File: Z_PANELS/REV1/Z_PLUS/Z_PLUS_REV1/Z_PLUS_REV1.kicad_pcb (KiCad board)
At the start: 4 copper layers, 98 x 98 mm, 47 parts, among them IC1 LTC4316IDD#PBF, J1 F3311A7H121014E200, Q1 BSS138, Q2 BSS138, Q3 MBT2222ADW1T1, Q4 BSS138, Q5 BSS138, Q6 MBT2222ADW1T1, U1 OPT4001DTST, U2 LTC3130EUDC-1-PBF

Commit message: made changes to Z plus board
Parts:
- removed D4: B220, Diode_SMD:D_SMB
- added D5: RB521S30T1G, AA_AUTO_LOADER:SODFL1608X70N, F.Cu at (171.5, 38.3)
- added D6: RB521S30T1G, AA_AUTO_LOADER:SODFL1608X70N, F.Cu at (179.9, 74.4)
- added D7: RB521S30T1G, AA_AUTO_LOADER:SODFL1608X70N, F.Cu at (176.2, 74.4)
- added IC2: SM141K04TFV, AA_AUTO_LOADER:SODFL490150X120N, F.Cu at (202.0, 103.0)
- added IC3: SM141K04TFV, AA_AUTO_LOADER:SODFL490150X120N, F.Cu at (137.8, 101.5)
- added IC4: SM141K04TFV, AA_AUTO_LOADER:SODFL490150X120N, F.Cu at (187.2, 48.1)
- added IC5: SM141K04TFV, AA_AUTO_LOADER:SODFL490150X120N, F.Cu at (186.7, 65.0)
- C1, C2, C3, C4, C5, C6, C7, C8, IC1, J1, L1, Q1, Q2, Q3, Q4, Q5, Q6, R1, R10, R11, R12, R13, R14, R15, R16, R17, R18, R19, R2, R20, R21, R22, R3, R4, R5, R6, R7, R8, R9, U2: moved to B.Cu
- D1, D3: value MBR0540-TP -> RB521S30T1G; footprint AA_AUTO_LOADER:SOD3716X135N -> AA_AUTO_LOADER:SODFL1608X70N
- D2: value B220 -> RB521S30T1G; footprint Diode_SMD:D_SMB -> AA_AUTO_LOADER:SODFL1608X70N; moved to B.Cu
- moved Q1 116.5 mm to (194.1, 61.0), turned to 180 degrees
- moved Q2 116.5 mm to (194.1, 65.4), turned to 180 degrees
- moved Q4 116.5 mm to (194.1, 69.9), turned to 180 degrees
- moved Q5 116.5 mm to (194.1, 74.3), turned to 180 degrees
- moved L1 115.3 mm to (193.5, 54.2), turned to 180 degrees
- moved R19 113.9 mm to (192.8, 49.5), turned to 180 degrees
- moved D2 113.0 mm to (192.4, 39.1), turned to 180 degrees
- moved R1 108.7 mm to (190.2, 59.8), turned to 180 degrees
- moved R10 108.7 mm to (190.2, 71.7), turned to 180 degrees
- moved R17 108.7 mm to (190.2, 73.7), turned to 180 degrees
- moved R2 108.7 mm to (190.2, 61.8), turned to 180 degrees
- moved R3 108.7 mm to (190.2, 63.7), turned to 180 degrees
- moved R4 108.7 mm to (190.2, 65.7), turned to 180 degrees
- moved R5 108.7 mm to (190.2, 67.7), turned to 180 degrees
- moved R6 108.7 mm to (190.2, 69.7), turned to 180 degrees
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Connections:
- C3 pad 2: Net-(D2-K) -> Net-(U2-PVIN)
- C4 pad 2: Net-(D2-K) -> Net-(U2-PVIN)
- C8 pad 2: Net-(D4-A) -> Net-(U2-VOUT)
- D1 pad 1: /SOLAR_PANEL_ELECTRONICS/7023_vout -> Net-(IC2-NEG)
- D1 pad 2: Net-(S1-Neg) -> Net-(IC3-NEG)
- D2 pad 1: Net-(D2-K) -> VSOLAR
- D2 pad 2: /SOLAR_PANEL_ELECTRONICS/7023_vout -> Net-(U2-VOUT)
- D3 pad 1: Net-(S1-Neg) -> /SOLAR_PANEL_ELECTRONICS/7023_vout
- D3 pad 2: GND -> Net-(IC2-NEG)
- J1 pad 12: VBATT -> unconnected-(J1-Pad12)
- J1 pad 13: VBATT -> unconnected-(J1-Pad13)
- J1 pad 2: VBATT -> unconnected-(J1-Pad2)
- J1 pad 3: VBATT -> unconnected-(J1-Pad3)
- R19 pad 2: Net-(D2-K) -> Net-(U2-PVIN)
- R21 pad 2: Net-(D4-A) -> Net-(U2-VOUT)
- U2 pad 14: Net-(D4-A) -> Net-(U2-VOUT)
- U2 pad 2: Net-(D2-K) -> Net-(U2-PVIN)
- U2 pad 3: Net-(D2-K) -> Net-(U2-PVIN)
- U2 pad 4: Net-(D2-K) -> Net-(U2-PVIN)
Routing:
- net Net-(IC2-NEG): track 0.00 -> 146.3 mm
- net Net-(IC3-NEG): track 0.00 -> 103.9 mm
- net Net-(IC4-NEG): track 0.00 -> 88.7 mm
- net GND: track 0.00 -> 20.9 mm
- net /SOLAR_PANEL_ELECTRONICS/7023_vout: track 0.00 -> 9.60 mm
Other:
- outline, holes or cut-outs redrawn

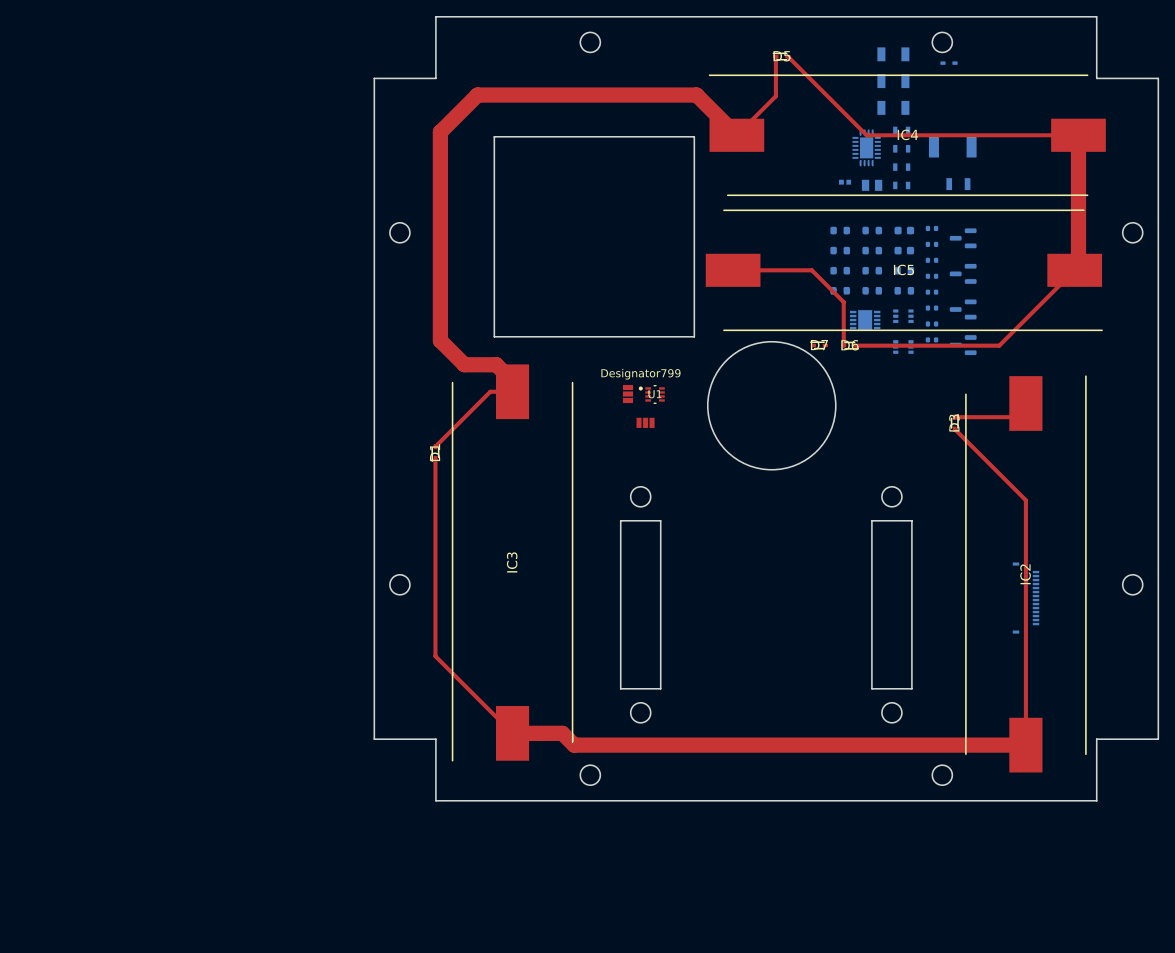
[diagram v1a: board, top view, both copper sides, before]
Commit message: initial routing z plus
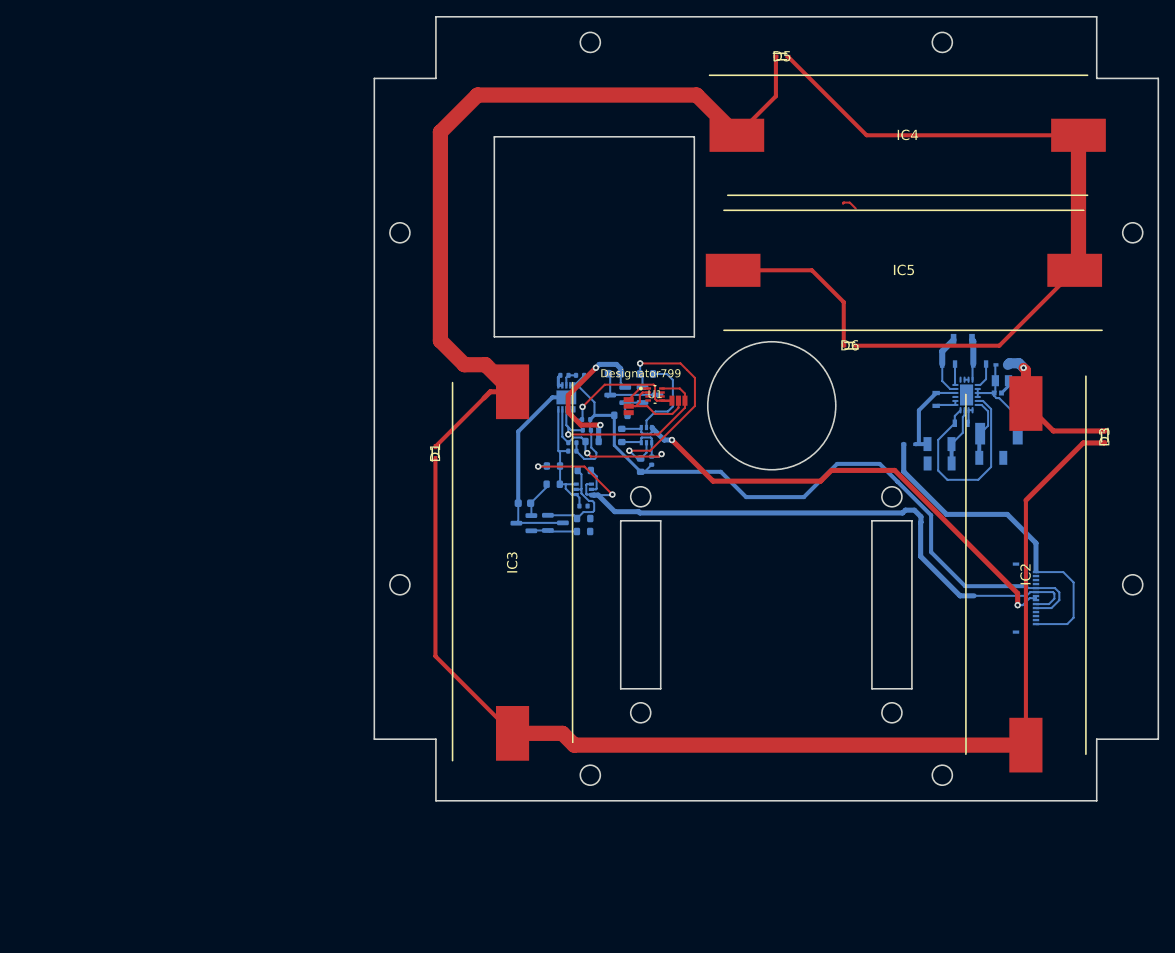
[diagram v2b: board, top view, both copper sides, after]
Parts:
- D7: moved to B.Cu
- moved Q2 63.1 mm to (139.2, 96.6)
- moved Q1 62.2 mm to (143.2, 96.6), turned to 0 degrees
- moved C1 58.4 mm to (139.3, 94.1)
- moved R20 51.9 mm to (197.6, 88.4)
- moved R7 51.7 mm to (146.7, 97.6), turned to 0 degrees
- moved R9 51.0 mm to (146.7, 96.0)
- moved R1 49.5 mm to (144.3, 78.1)
- moved R11 49.4 mm to (142.9, 91.7), turned to 0 degrees
- moved R10 49.1 mm to (146.7, 94.5), turned to 0 degrees
- moved R5 48.7 mm to (145.3, 86.5), turned to 0 degrees
- moved R6 48.4 mm to (145.3, 87.6), turned to 0 degrees
- moved D2 47.9 mm to (187.4, 86.7), turned to 0 degrees
- moved R3 47.6 mm to (147.0, 83.7), turned to 0 degrees
- moved R4 47.2 mm to (147.1, 85.0), turned to 0 degrees
- moved R2 46.9 mm to (146.2, 78.1)
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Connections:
- JP1 pad 1: unconnected-(JP1-A-Pad1) -> SDA_4001
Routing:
- net +3.3V: track 0.00 -> 98.8 mm
- net SCL1_b4iso: track 0.00 -> 86.5 mm, vias 0 -> 2
- net SDA1_b4iso: track 0.00 -> 65.2 mm, vias 0 -> 2
- net GND: track 20.9 -> 64.5 mm
- net VSOLAR: track 0.00 -> 41.8 mm
- net Net-(Q4-S): track 0.00 -> 28.9 mm, vias 0 -> 2
- net SDA_SUN: track 0.00 -> 26.3 mm, vias 0 -> 2
- net SDA_4001: track 0.00 -> 26.3 mm, vias 0 -> 1
- net Net-(U2-VCC): track 0.00 -> 25.8 mm
- net Net-(Q5-G): track 0.00 -> 19.9 mm, vias 0 -> 2
- net SCL_4001: track 0.00 -> 19.4 mm, vias 0 -> 1
- net SCL_SUN: track 0.00 -> 16.5 mm
- net Net-(U2-PVIN): track 0.00 -> 13.2 mm
- net Net-(Q1-S): track 0.00 -> 13.2 mm
- net Net-(JP1-C): track 0.00 -> 11.5 mm
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
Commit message: REV 1.0 ZPLUS
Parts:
- added .: ., logo:ARGUS_LOGO, F.Cu at (186.1, 78.9)
- added .: ., logo:ARGUS_LOGO, B.Cu at (201.8, 46.4)
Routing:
- net GND: track 64.5 -> 169.3 mm, vias 0 -> 262
- net Net-(Q1-S): track 13.2 -> 21.7 mm, vias 0 -> 2
- net +3.3V: track 98.8 -> 102.1 mm
- net (no net): track 2.05 -> 0.00 mm
- net Net-(Q1-G): track 5.77 -> 7.21 mm
- added copper zone on B.Cu, net GND
- added copper zone on F.Cu, net GND
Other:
- board text added: "Z-PLUS R1.0 ARGUS-1"
- board text added: "Z-PLUS REV 1.0 DESIGNED BY NISCHAL"
